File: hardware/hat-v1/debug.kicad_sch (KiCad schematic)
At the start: 41 parts, among them J5 Tag-Connect TC2050

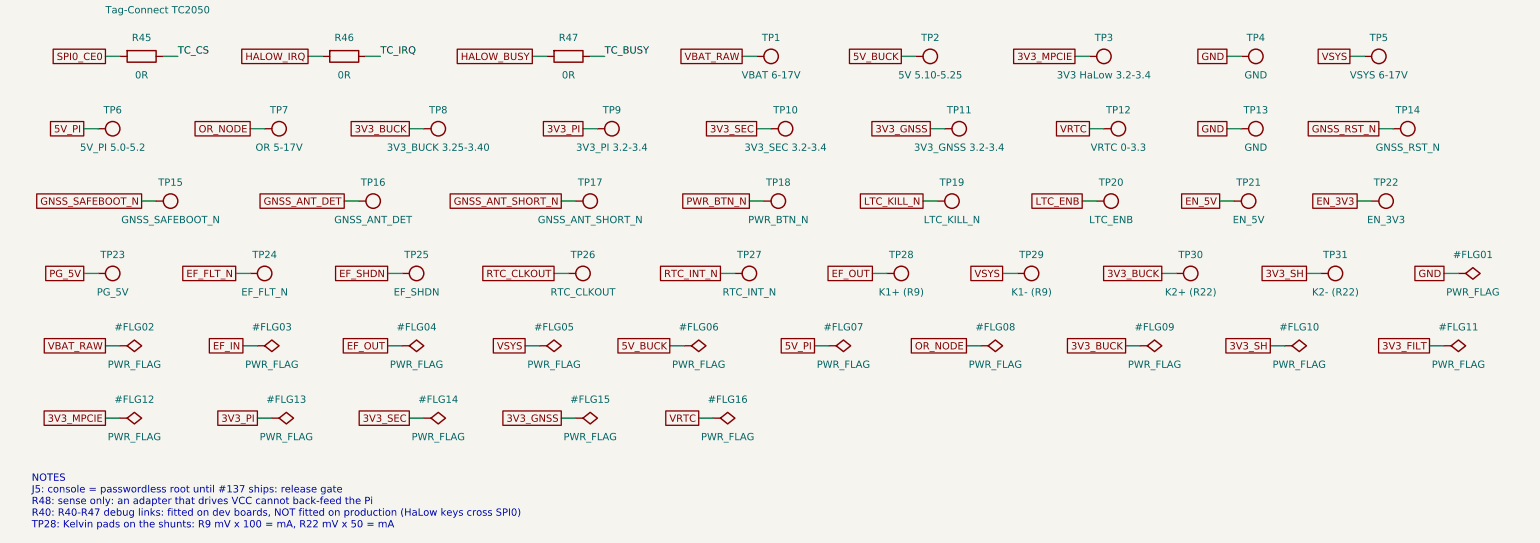
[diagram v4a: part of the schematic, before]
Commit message: HAT v1: option D power tree - HaLow 3.3 V buck fed from the Pi 5 V rail
- TPS62933F input moved from the OR node to 5V_PI (HAT 5 V buck or Pi USB-C),
  as on the WM1302 HAT: the HaLow card still runs on USB-C only
- EN pulled up to the Pi 3.3 V through 100k: no back-feed into an unpowered Pi,
  HAT+ STANDBY turns the card off; LTC2955 off already removes 5 V
- removed: LM74700 x2 + FET x2 + VCAP x2 (OR-ing), BENCH jumper + Q9/R24, Q8,
  HAT ID EEPROM + WP jumper + pull-ups + decoupling, OR_NODE test point
- kept the battery-present divider (spec review #22)
- checker: HaLow EN set points; spec 5.5.5 power tree review; re-placed board

Co-Authored-By: Claude Opus 5.5 <noreply@anthropic.com>
Claude-Session: https://claude.ai/code/session_01MLRuxTEmuMV82xcNLE62jW
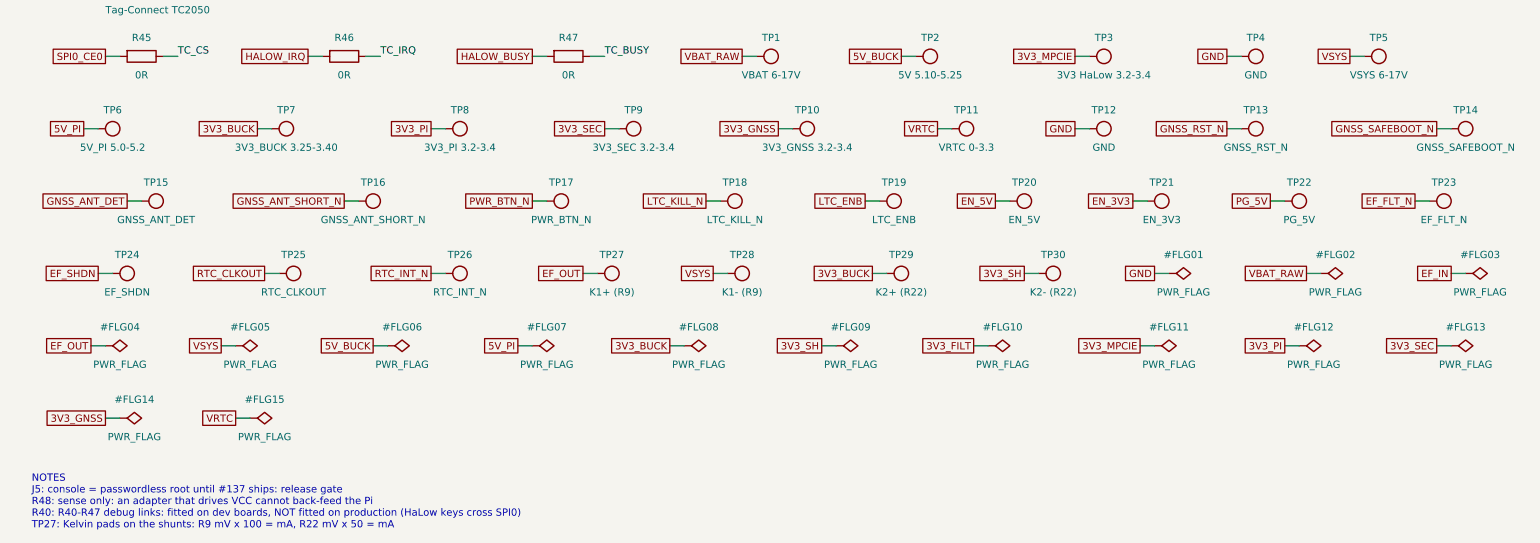
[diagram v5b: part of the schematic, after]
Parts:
- removed TP31: K2- (R22), TestPoint:TestPoint_Pad_D1.0mm, symbol batman:TP
- TP10: value 3V3_SEC 3.2-3.4 -> 3V3_GNSS 3.2-3.4
- TP11: value 3V3_GNSS 3.2-3.4 -> VRTC 0-3.3
- TP12: value VRTC 0-3.3 -> GND
- TP13: value GND -> GNSS_RST_N; footprint TestPoint:TestPoint_Pad_D1.5mm -> TestPoint:TestPoint_Pad_D1.0mm
- TP14: value GNSS_RST_N -> GNSS_SAFEBOOT_N
- TP15: value GNSS_SAFEBOOT_N -> GNSS_ANT_DET
- TP16: value GNSS_ANT_DET -> GNSS_ANT_SHORT_N
- TP17: value GNSS_ANT_SHORT_N -> PWR_BTN_N
- TP18: value PWR_BTN_N -> LTC_KILL_N
- TP19: value LTC_KILL_N -> LTC_ENB
- TP20: value LTC_ENB -> EN_5V
- TP21: value EN_5V -> EN_3V3
- TP22: value EN_3V3 -> PG_5V
- TP23: value PG_5V -> EF_FLT_N
- TP24: value EF_FLT_N -> EF_SHDN
- TP25: value EF_SHDN -> RTC_CLKOUT
- TP26: value RTC_CLKOUT -> RTC_INT_N
- TP27: value RTC_INT_N -> K1+ (R9); Note (none) -> Kelvin pads on the shunts: R9 mV x 100 = mA, R22 mV x 50 = 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
- TP28: value K1+ (R9) -> K1- (R9); Note Kelvin pads on the shunts: R9 mV x 100 = mA, R22 mV x 50 = 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 -> (none)
- TP29: value K1- (R9) -> K2+ (R22)
- TP30: value K2+ (R22) -> K2- (R22)
- TP7: value OR 5-17V -> 3V3_BUCK 3.25-3.40
- TP8: value 3V3_BUCK 3.25-3.40 -> 3V3_PI 3.2-3.4
- TP9: value 3V3_PI 3.2-3.4 -> 3V3_SEC 3.2-3.4
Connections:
- net OR_NODE is gone; now on net 3V3_BUCK: TP7.1
- net 3V3_BUCK: now also TP29.1; no longer TP30.1, TP8.1
- net 3V3_GNSS: now also TP10.1; no longer TP11.1
- net 3V3_PI: now also TP8.1; no longer TP9.1
- net 3V3_SEC: now also TP9.1; no longer TP10.1
- net 3V3_SH: now also TP30.1
- net EF_FLT_N: now also TP23.1; no longer TP24.1
- net EF_OUT: now also TP27.1; no longer TP28.1
- net EF_SHDN: now also TP24.1; no longer TP25.1
- net EN_3V3: now also TP21.1; no longer TP22.1
- net EN_5V: now also TP20.1; no longer TP21.1
- net GND: now also TP12.1; no longer TP13.1
- net GNSS_ANT_DET: now also TP15.1; no longer TP16.1
- net GNSS_ANT_SHORT_N: now also TP16.1; no longer TP17.1
- net GNSS_RST_N: now also TP13.1; no longer TP14.1
- net GNSS_SAFEBOOT_N: now also TP14.1; no longer TP15.1
- net LTC_ENB: now also TP19.1; no longer TP20.1
- net LTC_KILL_N: now also TP18.1; no longer TP19.1
- net PG_5V: now also TP22.1; no longer TP23.1
- net PWR_BTN_N: now also TP17.1; no longer TP18.1
- net RTC_CLKOUT: now also TP25.1; no longer TP26.1
- net RTC_INT_N: now also TP26.1; no longer TP27.1
- net VRTC: now also TP11.1; no longer TP12.1
- net VSYS: now also TP28.1; no longer TP29.1
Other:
- note added: "NOTES J5: console = passwordless root until #137 ships: release gate R48: sense only: an adapter that drives VCC cannot back-feed the Pi R40: R40-R47 debug links: fitted on dev boards, NOT fitted on production (HaLow keys cross SPI0) TP27: Kelvin pads on the shunts: R9 mV x 100 = mA, R22 mV x 50 = mA"
- note removed: "NOTES J5: console = passwordless root until #137 ships: release gate R48: sense only: an adapter that drives VCC cannot back-feed the Pi R40: R40-R47 debug links: fitted on dev boards, NOT fitted on production (HaLow keys cross SPI0) TP28: Kelvin pads on the shunts: R9 mV x 100 = mA, R22 mV x 50 = mA"
- moved on the sheet: TP10, TP11, TP12, TP14, TP15, TP17, TP18, TP19, TP20, TP21, TP22, TP23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
